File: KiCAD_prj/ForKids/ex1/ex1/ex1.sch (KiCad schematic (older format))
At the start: 3 parts

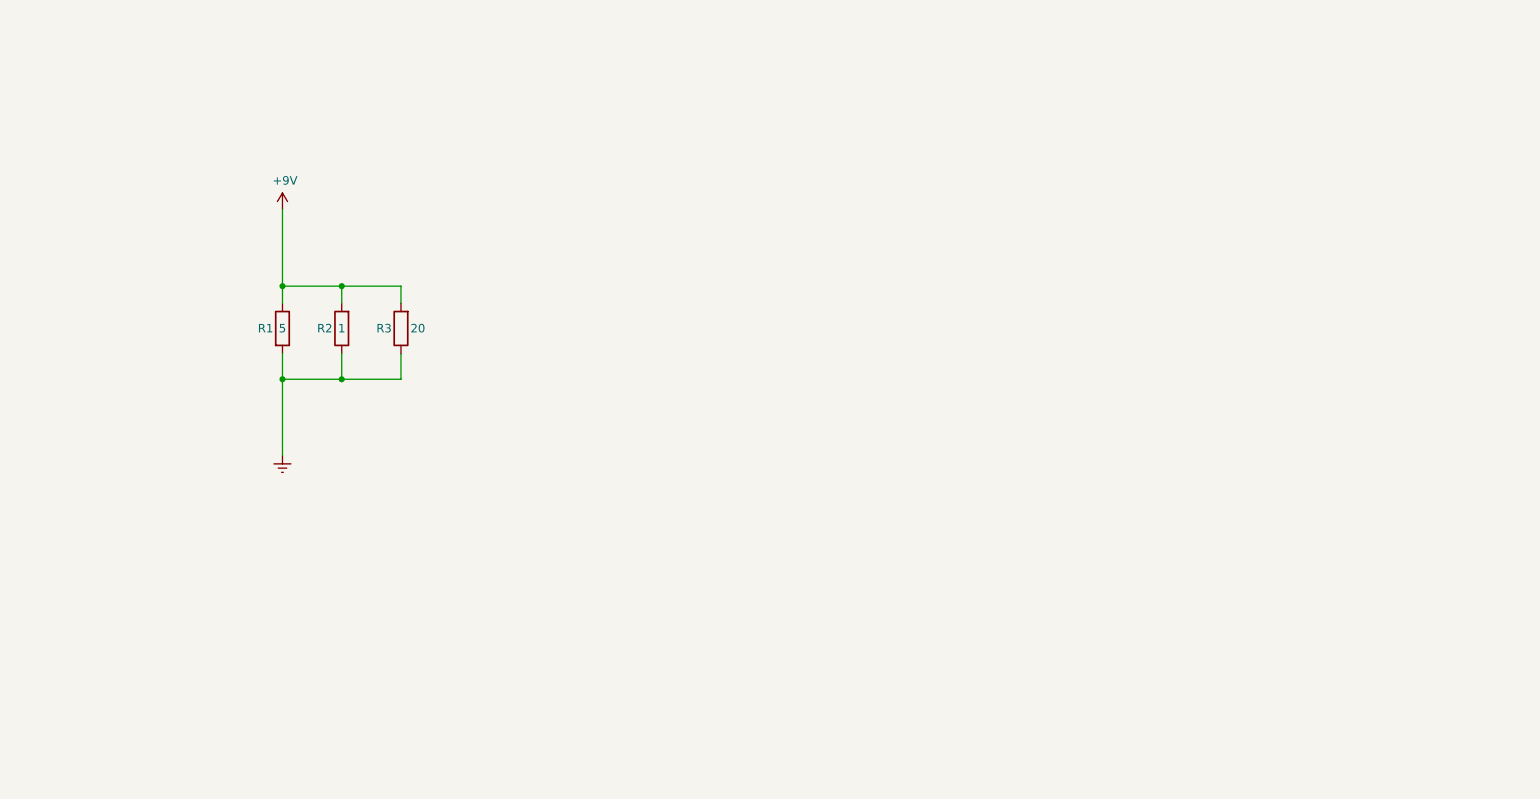
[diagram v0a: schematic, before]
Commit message: Added example project for my book
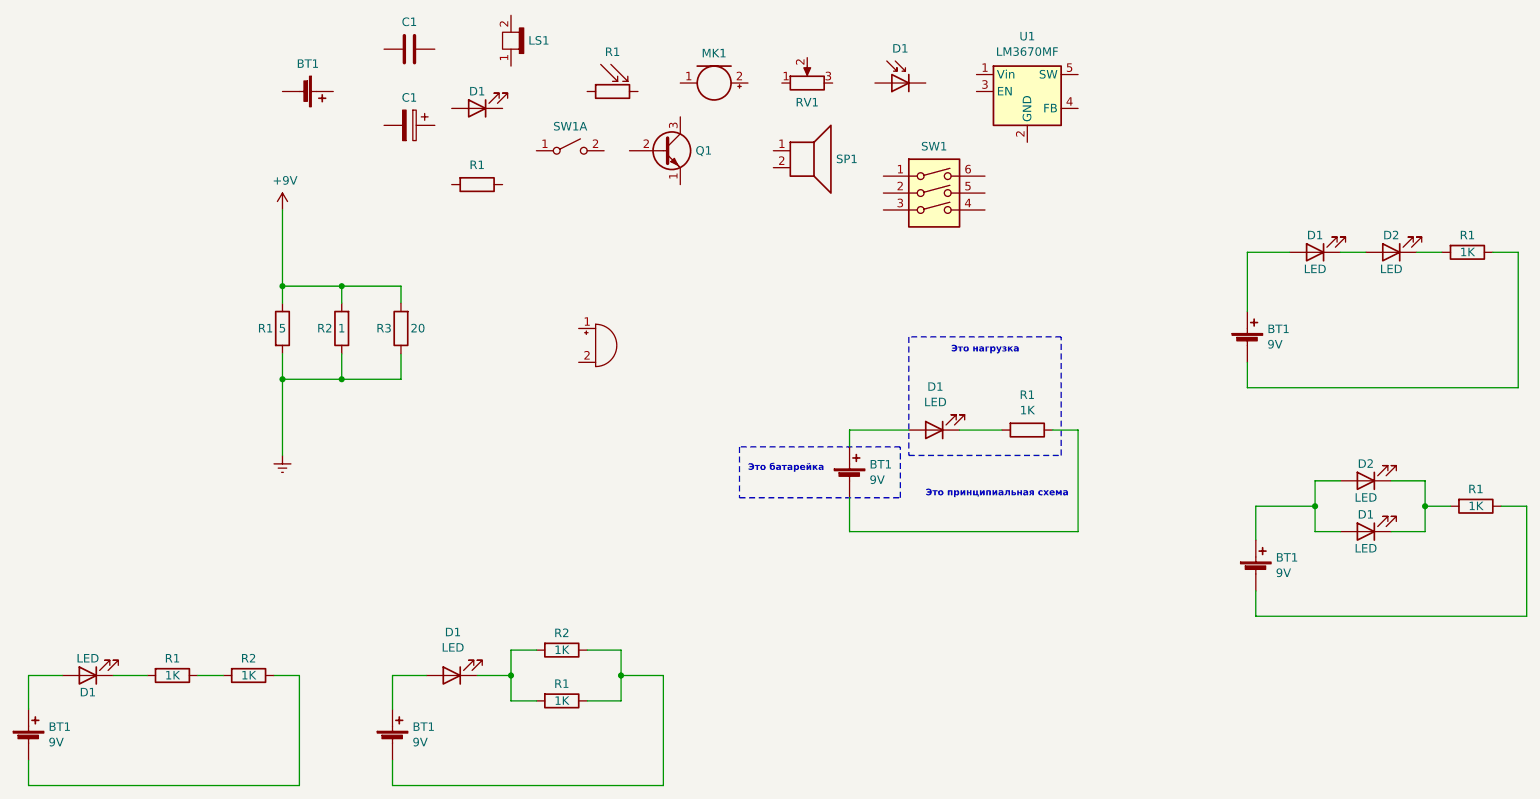
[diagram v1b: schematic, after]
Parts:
- added BT1: Battery_Cell, symbol Device:Battery_Cell
- added BT1 (x5): 9V, symbol Device:Battery_Cell
- added BZ?: Buzzer, symbol Device:Buzzer
- added C1: C, symbol Device:C
- added C1: CP, symbol Device:CP
- added D1 (x6), D2 (x2): LED, symbol Device:LED
- added D1: D_Photo, symbol Device:D_Photo
- added LS1: Earphone, symbol Device:Earphone
- added MK1: Microphone, symbol Device:Microphone
- added Q1: PN2222A, Package_TO_SOT_THT:TO-92_Inline, symbol Transistor_BJT:PN2222A
- added R1: R, symbol Device:R
- added R1: R_PHOTO, symbol Device:R_PHOTO
- added R1 (x5), R2 (x2): 1K, symbol Device:R
- added RV1: R_POT, symbol Device:R_POT
- added SP1: Speaker, symbol Device:Speaker
- added SW1: SW_DPST_x2, symbol Switch:SW_DPST_x2
- added SW1: SW_DIP_x03, symbol Switch:SW_DIP_x03
- added U1: LM3670MF, Package_TO_SOT_SMD:TSOT-23-5, symbol Regulator_Switching:LM3670MF
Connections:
- new net: BT1.1 (+), D1.2 (A) (x4)
- new net: BT1.2 (-), R1.1 (x3)
- new net: D1.1 (K), R1.2 (x2)
- new net: D2.1 (K), R1.2
- new net: D1.1 (K), D2.2 (A)
- new net: BT1.1 (+), D1.2 (A), D2.2 (A)
- new net: D1.1 (K), D2.1 (K), R1.2
- new net: BT1.2 (-), R1.1, R2.1
- new net: D1.1 (K), R1.2, R2.2
- new net: BT1.2 (-), R2.1
- new net: R1.1, R2.2
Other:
- note added: "Это батарейка"
- note added: "Это нагрузка"
- note added: "Это принципиальная схема"
